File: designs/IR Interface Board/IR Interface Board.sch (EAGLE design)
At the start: 67 parts, among them IC2 PIC16F1517/19PT, IC4 REG1118

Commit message: Fix Resistor values
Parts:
- R13, R15, R16, R21, R3, R6, R7: value 10K -> 500
- R2: value 330 -> 500
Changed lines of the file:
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@@
 <?xml version="1.0" encoding="utf-8"?>
 <!DOCTYPE eagle SYSTEM "eagle.dtd">
-<eagle version="7.4.0">
+<eagle version="7.6.0">
 <drawing>
 <settings>
@@
 <part name="LED2" library="interface_board-rev13" deviceset="LED" device="SML0603"/>
 <part name="LED3" library="interface_board-rev13" deviceset="LED" device="SML0603"/>
-<part name="R6" library="rcl" deviceset="R-US_" device="R1206" value="10K"/>
-<part name="R7" library="rcl" deviceset="R-US_" device="R1206" value="10K"/>
+<part name="R6" library="rcl" deviceset="R-US_" device="R1206" value="500"/>
+<part name="R7" library="rcl" deviceset="R-US_" device="R1206" value="500"/>
 <part name="C5" library="rcl" deviceset="C-US" device="C0805" value="0.1uF"/>
 <part name="C6" library="rcl" deviceset="C-US" device="C0805" value="0.1uF"/>
@@
 <part name="C20" library="rcl" deviceset="C-US" device="C0805" value="0.1uF"/>
 <part name="LED4" library="interface_board-rev13" deviceset="LED" device="SML0603"/>
-<part name="R21" library="rcl" deviceset="R-US_" device="R1206" value="10K"/>
+<part name="R21" library="rcl" deviceset="R-US_" device="R1206" value="500"/>
 <part name="JP11" library="pinhead" deviceset="PINHD-1X6" device="/90"/>
 <part name="R9" library="rcl" deviceset="R-US_" device="R1206" value="100"/>
@@
 <part name="GND39" library="supply1" deviceset="GND" device=""/>
 <part name="LED6" library="interface_board-rev13" deviceset="LED" device="SML0603"/>
-<part name="R13" library="rcl" deviceset="R-US_" device="R1206" value="10K"/>
+<part name="R13" library="rcl" deviceset="R-US_" device="R1206" value="500"/>
 <part name="LED8" library="interface_board-rev13" deviceset="LED" device="SML0603"/>
-<part name="R15" library="rcl" deviceset="R-US_" device="R1206" value="10K"/>
+<part name="R15" library="rcl" deviceset="R-US_" device="R1206" value="500"/>
 <part name="LED9" library="interface_board-rev13" deviceset="LED" device="SML0603"/>
-<part name="R16" library="rcl" deviceset="R-US_" device="R1206" value="10K"/>
+<part name="R16" library="rcl" deviceset="R-US_" device="R1206" value="500"/>
 <part name="FRAME3" library="frames" deviceset="FRAME_A_L" device=""/>
 <part name="OUT0" library="pinhead" deviceset="PINHD-1X4" device=""/>
@@
 <part name="RST_JMPR1" library="con-lstb" deviceset="MA03-1" device=""/>
 <part name="R1" library="resistor" deviceset="R-US_" device="R0805" value="1k"/>
-<part name="R2" library="resistor" deviceset="R-US_" device="R0805" value="330"/>
+<part name="R2" library="resistor" deviceset="R-US_" device="R0805" value="500"/>
 <part name="GND1" library="supply1" deviceset="GND" device=""/>
 <part name="C8" library="resistor" deviceset="C-EU" device="C0805" value="0.1uF"/>
@@
 <part name="C11" library="rcl" deviceset="C-US" device="C0805" value="4.7 uF"/>
 <part name="LED1" library="interface_board-rev13" deviceset="LED" device="SML0603"/>
-<part name="R3" library="rcl" deviceset="R-US_" device="R1206" value="10K"/>
+<part name="R3" library="rcl" deviceset="R-US_" device="R1206" value="500"/>
 <part name="OUT20" library="pinhead" deviceset="PINHD-1X4" device=""/>
 <part name="OUT21" library="pinhead" deviceset="PINHD-1X4" device=""/>

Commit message: Fiexd +5 V
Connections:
- removed net BT_VBUS1: BT_FTDI1.VBUS, BT_USB_MICROB1.VBUS, R2.2
- net +5V: now also BT_FTDI1.VBUS, BT_USB_MICROB1.VBUS, R2.2
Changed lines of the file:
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@@
 <label x="243.84" y="114.3" size="1.27" layer="95" rot="R90" xref="yes"/>
+</segment>
+<segment>
+<pinref part="R2" gate="G$1" pin="2"/>
+<pinref part="BT_USB_MICROB1" gate="G$1" pin="VBUS"/>
+<wire x1="21.59" y1="66.04" x2="26.67" y2="66.04" width="0.1524" layer="91"/>
+<wire x1="26.67" y1="66.04" x2="26.67" y2="83.82" width="0.1524" layer="91"/>
+<pinref part="BT_FTDI1" gate="G$1" pin="VBUS"/>
+<wire x1="55.88" y1="83.82" x2="26.67" y2="83.82" width="0.1524" layer="91"/>
+<wire x1="26.67" y1="60.96" x2="26.67" y2="66.04" width="0.1524" layer="91"/>
+<junction x="26.67" y="66.04"/>
 </segment>
 </net>
@@
 </segment>
 </net>
-<net name="BT_VBUS1" class="0">
-<segment>
-<pinref part="R2" gate="G$1" pin="2"/>
-<pinref part="BT_USB_MICROB1" gate="G$1" pin="VBUS"/>
-<wire x1="21.59" y1="66.04" x2="26.67" y2="66.04" width="0.1524" layer="91"/>
-<wire x1="26.67" y1="66.04" x2="26.67" y2="83.82" width="0.1524" layer="91"/>
-<pinref part="BT_FTDI1" gate="G$1" pin="VBUS"/>
-<wire x1="55.88" y1="83.82" x2="26.67" y2="83.82" width="0.1524" layer="91"/>
-<wire x1="26.67" y1="60.96" x2="26.67" y2="66.04" width="0.1524" layer="91"/>
-<junction x="26.67" y="66.04"/>
-</segment>
-</net>

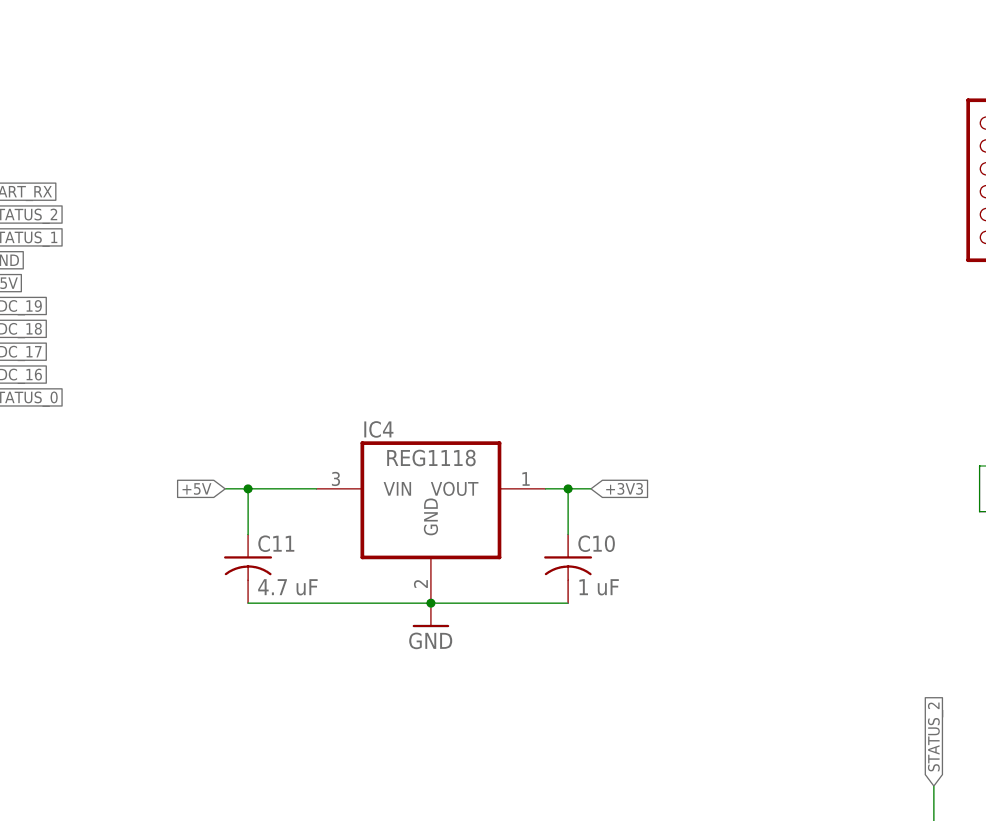
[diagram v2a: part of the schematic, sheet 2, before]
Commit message: Finished layout. Kind of rushed. Probably needs a second set of eyes.
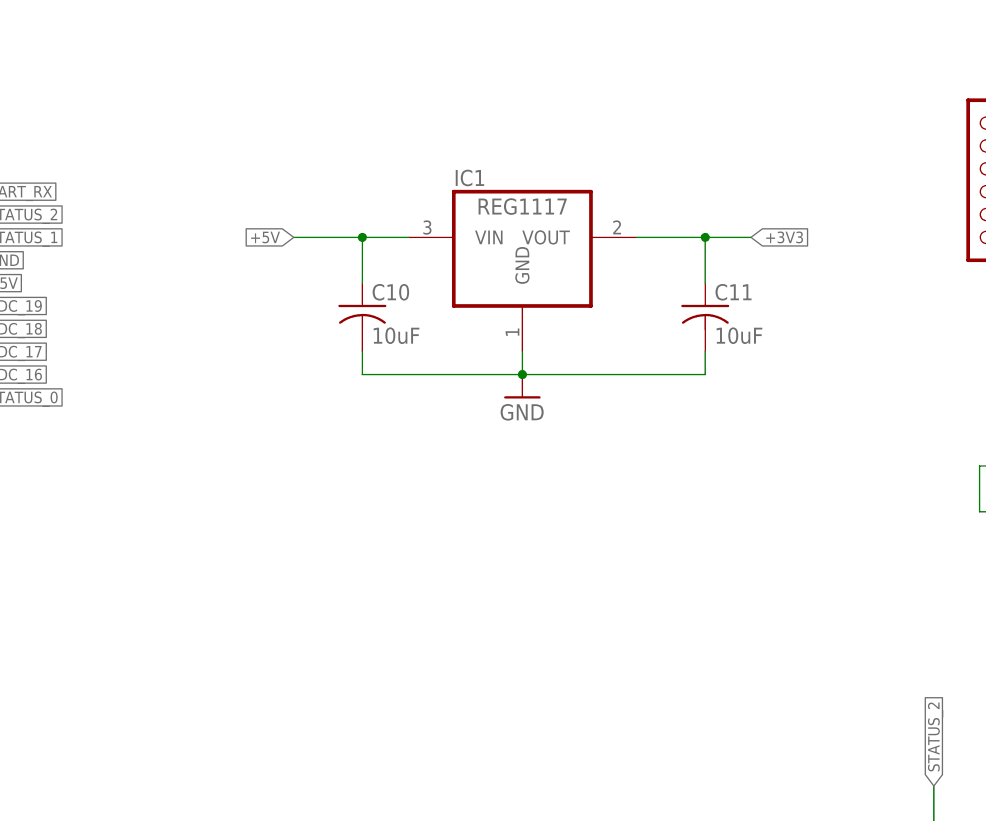
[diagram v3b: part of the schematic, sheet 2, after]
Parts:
- removed IC4: REG1118, burr-brown:REG1118
- added H1, H2, H3, H4: MOUNT-PAD-ROUND3.2, holes:MOUNT-PAD-ROUND3.2
- added IC1: REG1117, burr-brown:REG1117
- added JP1, JP2: (no value), pinhead:PINHD-1X2
- C10: value 1 uF -> 10uF
- C11: value 4.7 uF -> 10uF
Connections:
- new net VBUS: BT_FTDI1.VBUS, BT_USB_MICROB1.VBUS, JP2.1, R2.2
- net +3V3: now also C11.1, IC1.VOUT; no longer C10.1, IC4.VOUT
- net +5V: now also C10.1, IC1.VIN, JP1.1; no longer BT_FTDI1.VBUS, BT_USB_MICROB1.VBUS, C11.1, IC4.VIN, R2.2
- net GND: now also H1.MOUNT, H2.MOUNT, H3.MOUNT, H4.MOUNT, IC1.GND, JP1.2, JP2.2; no longer IC4.GND
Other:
- moved on the sheet: C10, C11

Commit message: Done with Unknown
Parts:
- removed FTDI1: (no value), interface_board-rev13:LEDCHIPLED_1206
- added C12: 10uF, rcl:C-USC0805
- added LED5: (no value), interface_board-rev13:LEDSML0603
- C1, C2, C8, C9: device resistor:C-EUC0805 -> rcl:C-USC0805
- C11: value 10uF -> 4.7uF
- C20, C5: value 0.1uF -> 1uF
- C3, C4, C6: value 0.1uF -> 4.7uF
- R10, R13, R15, R16, R21, R3, R6, R7, R9: device rcl:R-US_R1206 -> rcl:R-US_R0805
- R2: device resistor:R-US_R0805 -> rcl:R-US_R0805
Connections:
- removed net GND1: LED6.C
- net +3V3: now also R15.2, R16.2
- net +5V: now also C12.1, JP2.2; no longer R15.2, R16.2
- net ADC_10: now also IC2.CCP2/AN9/RB3; no longer IC2.AN11/RB4
- net ADC_11: now also IC2.!SS!/AN0/RA0; no longer IC2.T1G/AN13/RB5
- net ADC_12: now also IC2.T1G/AN13/RB5; no longer IC2.!SS!/AN0/RA0
- net ADC_13: now also IC2.AN2/RA2; no longer IC2.AN1/RA1
- net ADC_14: now also IC2.AN1/RA1; no longer IC2.AN2/RA2
- net ADC_15: now also IC2.RA5/AN4/!SS!/VCAP; no longer IC2.VREF+/AN3/RA3
- net ADC_16: now also IC2.VREF+/AN3/RA3; no longer IC2.RA5/AN4/!SS!/VCAP
- net ADC_17: now also IC2.RE1/AN6; no longer IC2.RE0/AN5
- net ADC_18: now also IC2.RE0/AN5; no longer IC2.RE1/AN6
- net ADC_19: now also IC2.RC2/AN14/CCP1; no longer IC2.RE2/AN7
- net ADC_20: now also IC2.RE2/AN7; no longer IC2.RC2/AN14/CCP1
- net ADC_21: now also IC2.RD0/AN20; no longer IC2.RC3/AN15/SCK/SCL
- net ADC_22: now also IC2.RC3/AN15/SCK/SCL; no longer IC2.RD0/AN20
- net ADC_23: now also IC2.RD2/AN22; no longer IC2.RD1/AN21
- net ADC_24: now also IC2.RD1/AN21; no longer IC2.RD2/AN22
- net ADC_25: now also IC2.RC4/AN16/SDI/SDA; no longer IC2.RD3/AN23
- net ADC_26: now also IC2.RD3/AN23; no longer IC2.RC4/AN16/SDI/SDA
- net ADC_27: now also IC2.RC6/AN18/TX/CK; no longer IC2.RC5/AN17/SDO
- net ADC_28: now also IC2.RC5/AN17/SDO; no longer IC2.RC6/AN18/TX/CK
- net ADC_3: now also IC2.AN26/RD6; no longer IC2.AN25/RD5
- net ADC_4: now also IC2.AN25/RD5; no longer IC2.AN26/RD6
- net ADC_5: now also IC2.INT/AN12/RB0; no longer IC2.AN27/RD7
- net ADC_6: now also IC2.AN27/RD7; no longer IC2.INT/AN12/RB0
- net ADC_7: now also IC2.AN8/RB2; no longer IC2.AN10/RB1
- net ADC_8: now also IC2.AN10/RB1; no longer IC2.AN8/RB2
- net ADC_9: now also IC2.AN11/RB4; no longer IC2.CCP2/AN9/RB3
- net GND: now also C12.2, LED5.C, LED6.C; no longer FTDI1.C, JP2.2
- net N$12: now also LED5.A; no longer FTDI1.A

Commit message: done with first version of the boards
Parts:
- added U$1: LOGO, IEEE-logo:LOGO
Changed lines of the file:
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@@
 <part name="LED5" library="interface_board-rev13" deviceset="LED" device="SML0603"/>
 <part name="C12" library="rcl" deviceset="C-US" device="C0805" value="10uF"/>
+<part name="U$1" library="IEEE-logo" deviceset="LOGO" device=""/>
 </parts>
 <sheets>
@@
 <instance part="LED5" gate="G$1" x="26.67" y="45.72"/>
 <instance part="C12" gate="G$1" x="132.08" y="93.98"/>
+<instance part="U$1" gate="G$1" x="129.54" y="127"/>
 </instances>
 <busses>
